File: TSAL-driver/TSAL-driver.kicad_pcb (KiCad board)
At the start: 2 copper layers, 20.3 x 56.5 mm, 12 parts, among them J1 LED+, J2 LED-, J3 12V, J4 GND, U1 AZ1117-5.0, U2 ATtiny25-20SSU, U3 LDB-350L

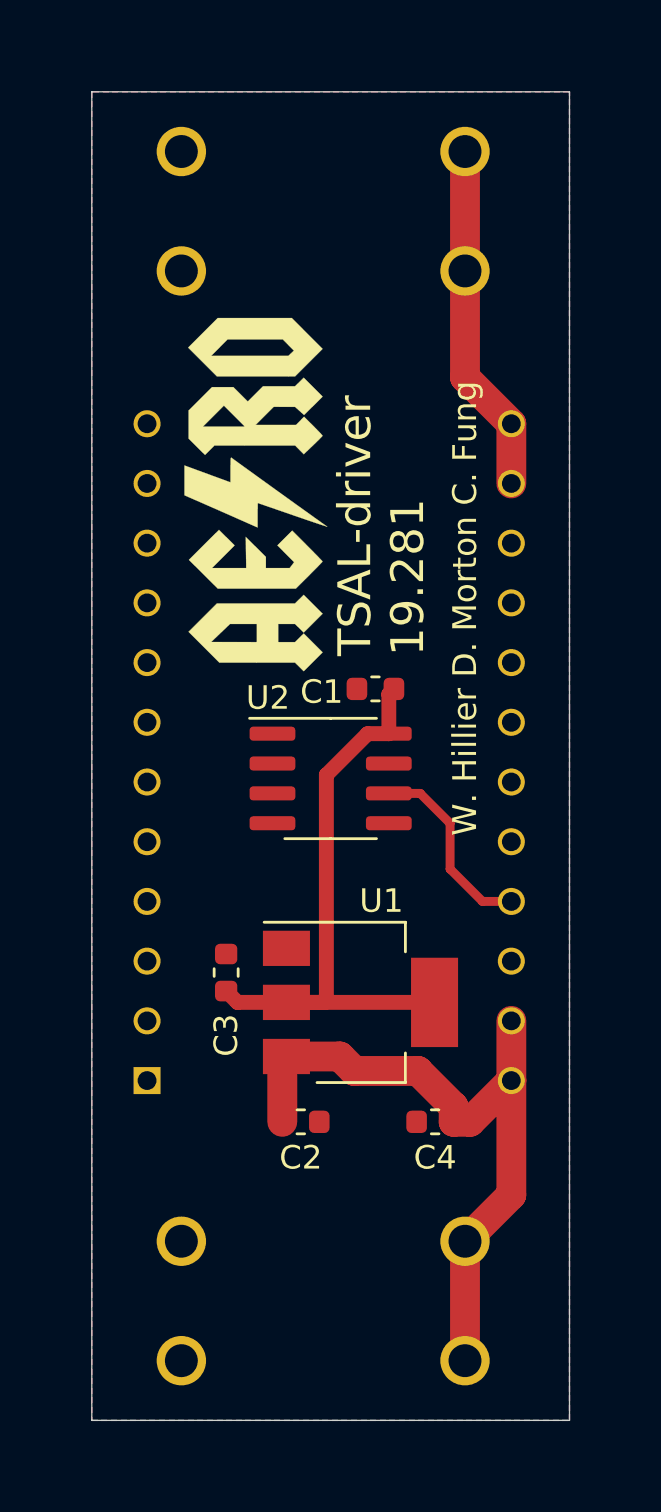
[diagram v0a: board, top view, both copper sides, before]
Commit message: New LDB footprint
Completed TSAL
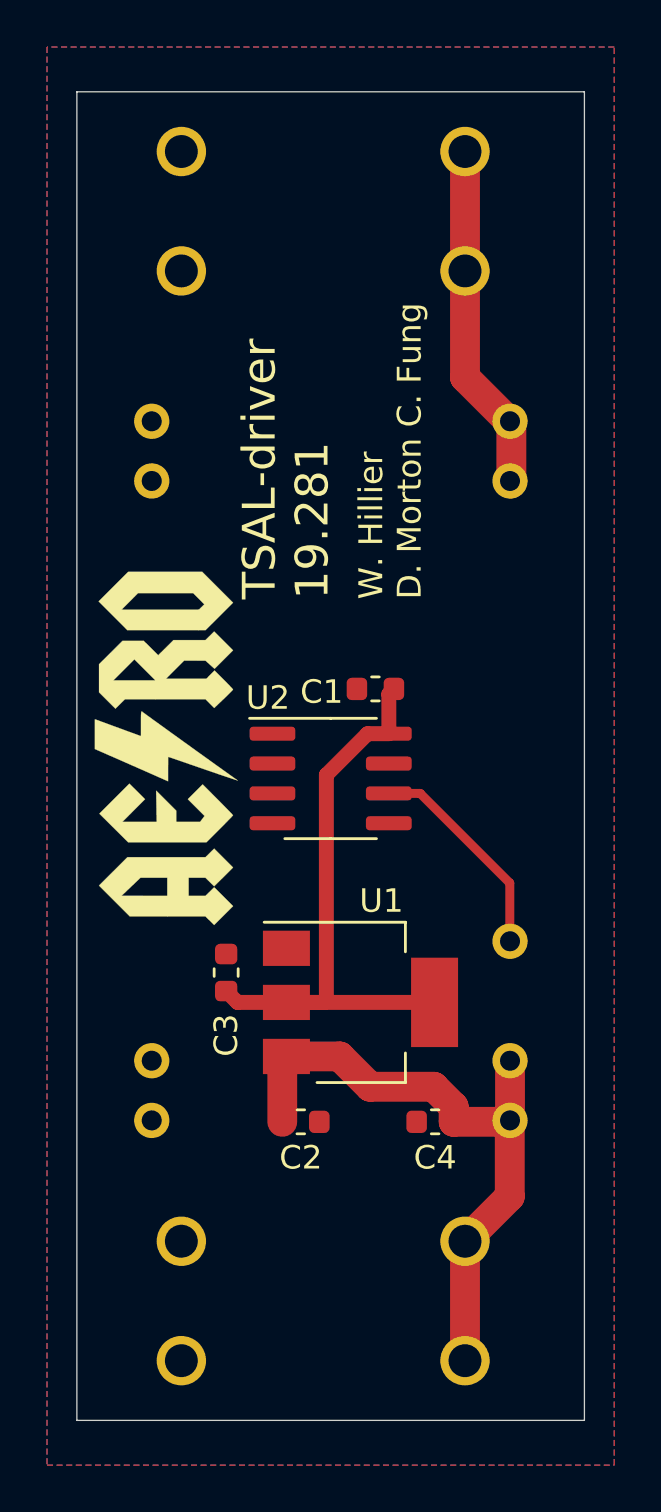
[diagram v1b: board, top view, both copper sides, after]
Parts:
- U3: footprint AERO-footprints:DIP1549W45P254L3404H940Q24 -> AERO-footprints:LDB-_L
- moved U3 16.0 mm to (126.4, 71.8)
- moved G*** 11.4 mm to (127.0, 85.7)
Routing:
- net +12V: track 29.9 -> 27.5 mm
- net /PWM_DIM: track 8.25 -> 9.21 mm
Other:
- board size 20.3 x 56.5 mm -> 21.6 x 56.5 mm
